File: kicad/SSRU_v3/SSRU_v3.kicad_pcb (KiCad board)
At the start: 2 copper layers, 100 x 100 mm, 115 parts, among them J1 AVR-ISP-6, J10 Conn_01x04, J11 Conn_01x02, J20 Conn_01x02, J21 Conn_01x02, J22 Conn_01x04, J23 Conn_01x02, J24 Conn_01x04, J25 Conn_01x02, J26 Conn_01x03, J27 Conn_01x03, J3 Conn_01x02, J30 Conn_01x02, J31 Conn_01x04, J32 Conn_01x04, J4 Conn_01x02, J5 Conn_01x02, SW1 SW_Push, U1 MCP2515-xSO, U10 TJA1051T, U11 Ai-Thinker-Ra-02, U12 TJA1051T, U13 CH340N, U2 ATmega328P-A, U3 TXS0102DCT, U4 LM2576S-5, U5 AMS1117-3.3, U6 LM324, U7 MCP2515-xSO, U8 74LVC1G17, U9 MT3608/SDB628, Y1 16MHz, Y3 16MHz, Y4 16MHz

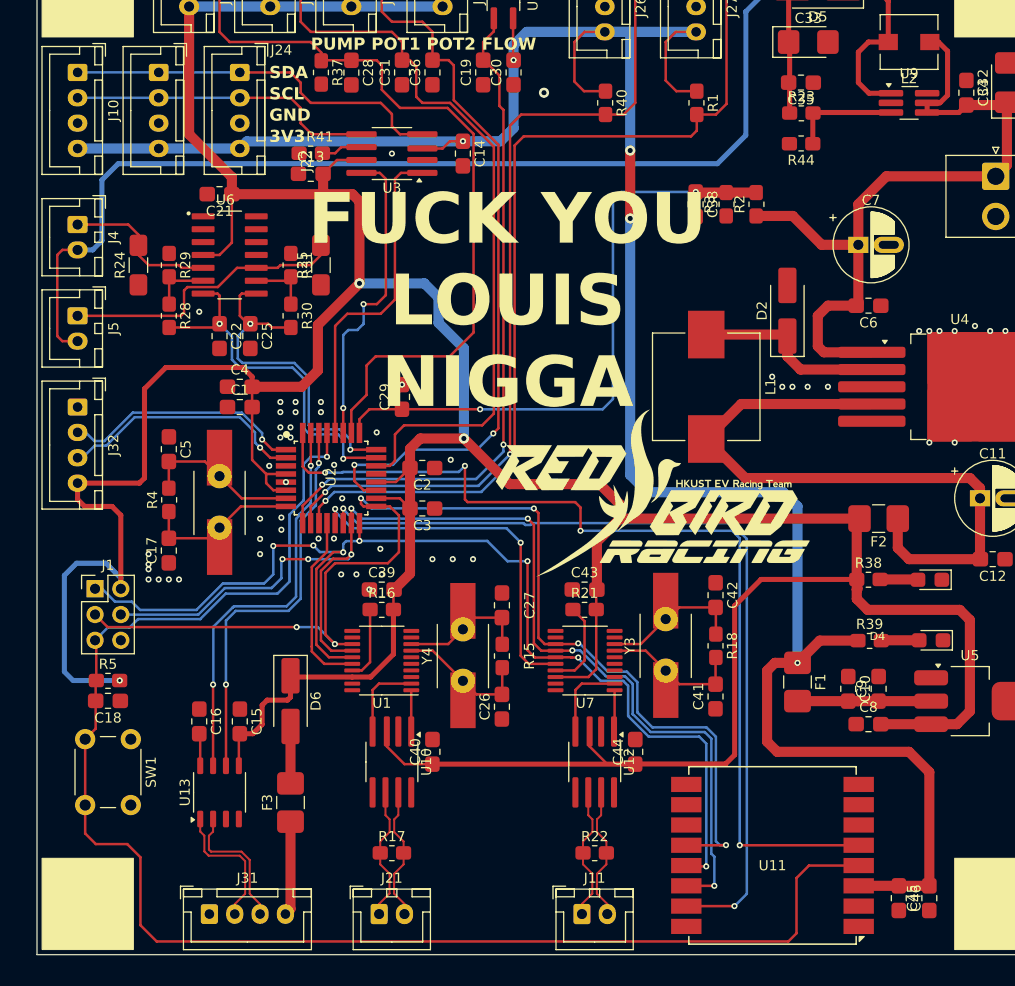
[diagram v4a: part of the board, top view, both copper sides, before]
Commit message: created TS schematics
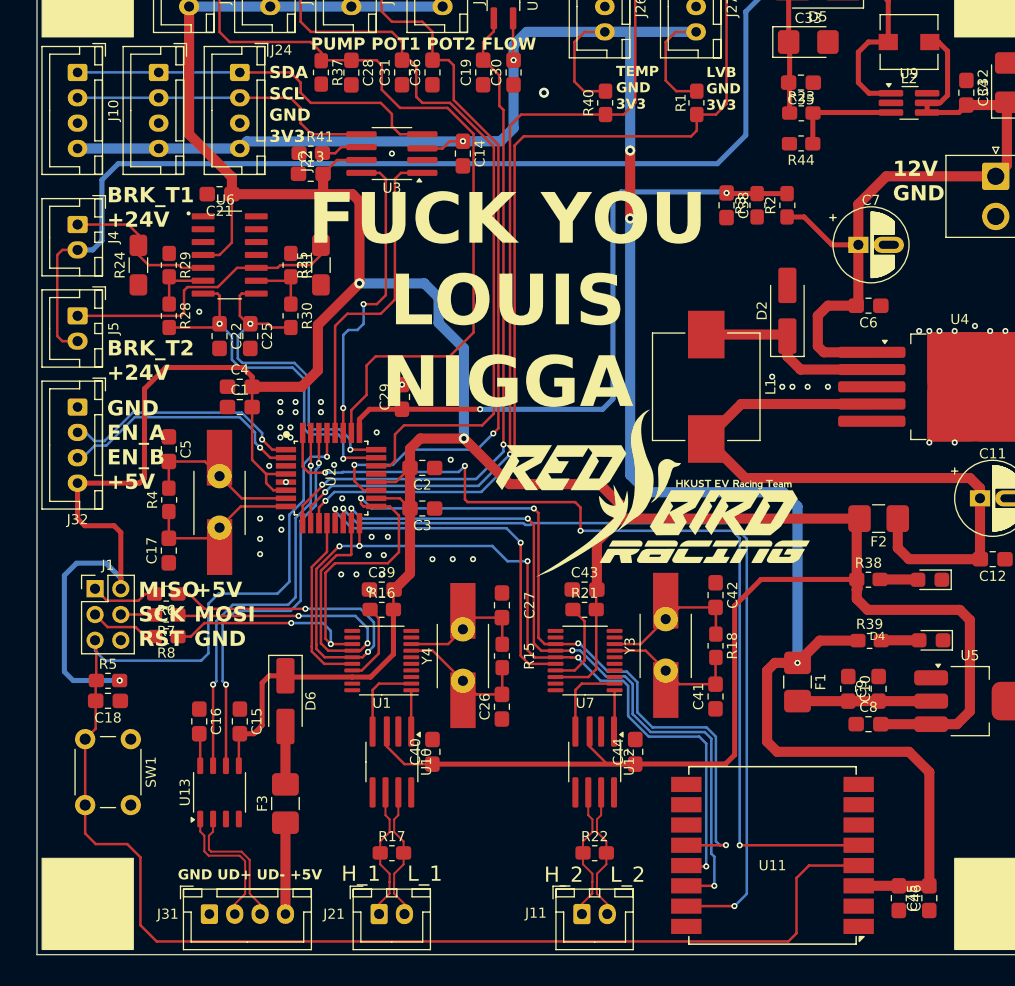
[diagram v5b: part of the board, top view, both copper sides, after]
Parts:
- added R6: 4.7k, RMC_Resistor:R_0805_2012Metric_Pad1.20x1.40mm_HandSolder_L, F.Cu at (112.7, 114.4)
- added R7: 4.7k, RMC_Resistor:R_0805_2012Metric_Pad1.20x1.40mm_HandSolder_L, F.Cu at (112.7, 116.5)
- added R8: 4.7k, RMC_Resistor:R_0805_2012Metric_Pad1.20x1.40mm_HandSolder_L, F.Cu at (112.7, 118.6)
- moved C38 3.05 mm to (168.0, 76.1)
- moved R2 3.05 mm to (174.0, 76.1)
- moved R3 3.05 mm to (171.0, 76.1)
- moved F3 0.51 mm to (124.5, 135.1)
- moved D6 0.50 mm to (124.5, 125.0)
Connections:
- J1 pad 1: MISO -> Net-(J1-MISO)
- J1 pad 3: SCK -> Net-(J1-SCK)
- J1 pad 4: MOSI -> Net-(J1-MOSI)
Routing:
- net SCK: track 119.6 -> 112.2 mm
- net Net-(J1-SCK): track 0.00 -> 6.77 mm
- net Net-(J1-MISO): track 0.00 -> 6.64 mm
- net RST: track 149.2 -> 154.3 mm
- net MISO: track 112.6 -> 107.9 mm
- net MOSI: track 115.8 -> 112.2 mm, vias 7 -> 6
- net Net-(J1-MOSI): track 0.00 -> 3.34 mm
- net +12V: track 74.6 -> 71.5 mm
- net LVB_S: track 61.3 -> 64.3 mm
- net Net-(U1-~{RESET}): track 7.29 -> 7.99 mm
- net GND: vias 68 -> 62
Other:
- board text added: "+5V MOSI GND"
- board text added: "12V GND"
- board text added: "BRK_T1 +24V"
- board text added: "BRK_T2 +24V"
- board text added: "GND EN_A EN_B +5V"
- board text added: "GND UD+ UD- +5V"
- board text added: "H_1 L_1"
- board text added: "H_2 L_2"
- board text added: "LVB GND 3V3"
- board text added: "MISO SCK RST"
- board text added: "TEMP GND 3V3"

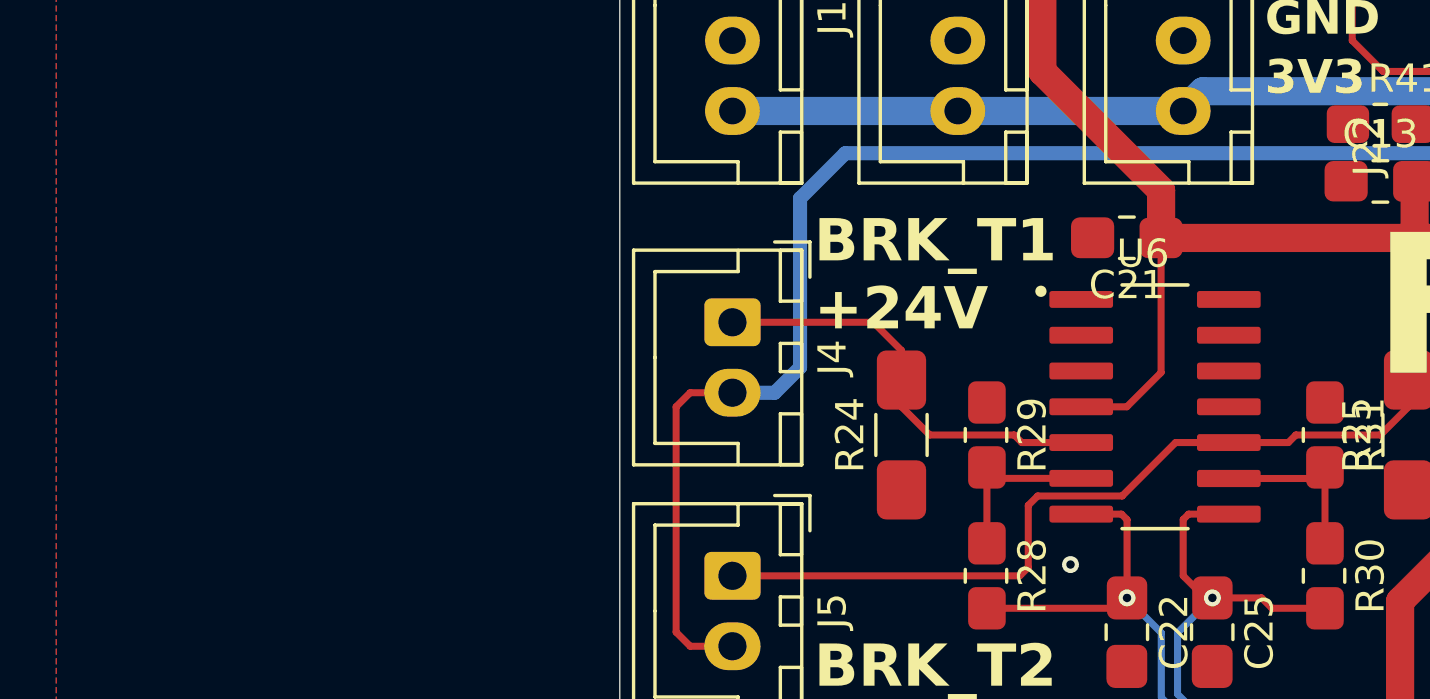
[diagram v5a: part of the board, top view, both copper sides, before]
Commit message: current to voltage
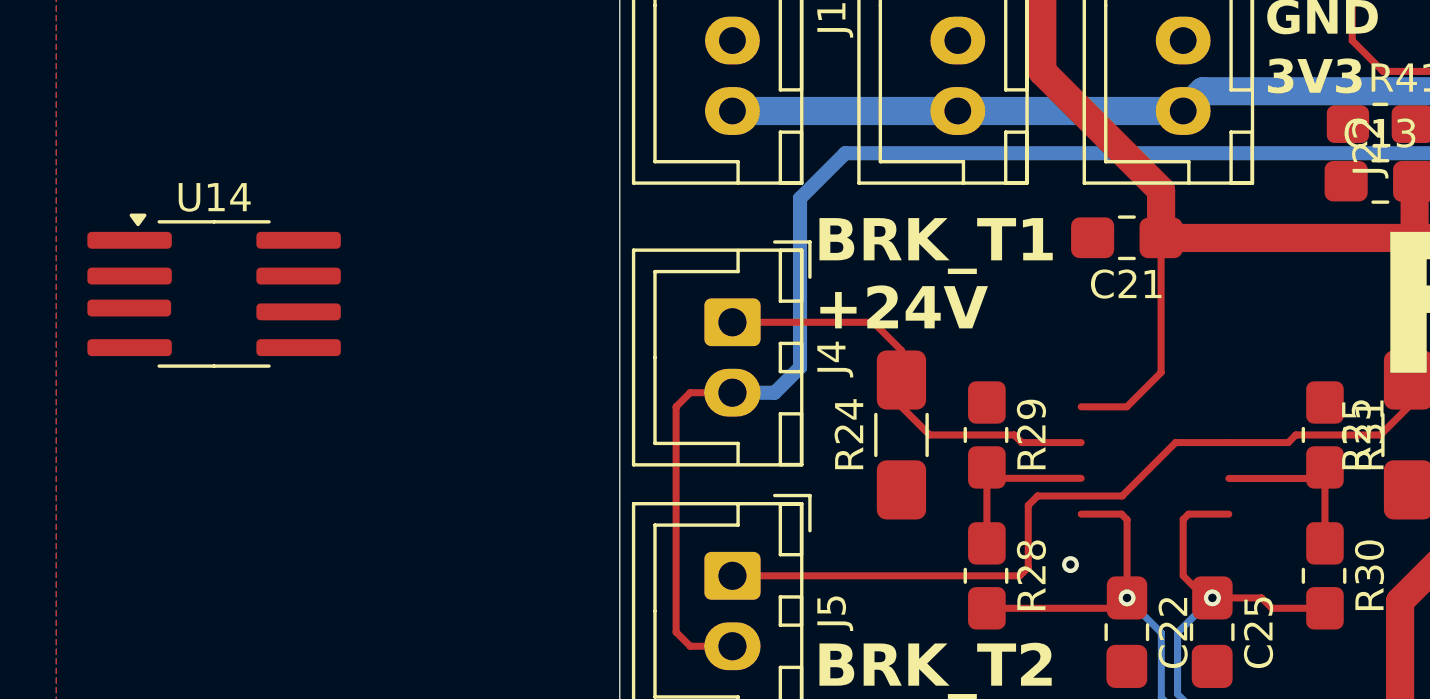
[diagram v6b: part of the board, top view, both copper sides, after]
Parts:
- removed U6: LM324, RMC_SO:SOIC127P600X175-14N
- added U14: LM2904, RMC_SO:SOIC-8_3.9x4.9mm_P1.27mm_RMC_Handsolder, F.Cu at (85.6, 77.0)

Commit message: SSRU V3
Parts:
- removed J10: Conn_01x04, Connector_JST:JST_XH_B4B-XH-A_1x04_P2.50mm_Vertical
- added G***: LOGO, LOGO, F.Cu at (147.0, 83.8)
- added G***: LOGO, LOGO, B.Cu at (150.0, 99.8)
- R28: value 5k -> 22k
- moved U14 33.5 mm to (119.0, 80.0), turned to 180 degrees
- moved C21 9.18 mm to (116.2, 84.0)
- moved J22 8.00 mm to (104.0, 63.0)
- moved J24 5.00 mm to (115.0, 63.0)
- moved G*** 4.24 mm to (157.0, 103.0)
- moved C41 0.93 mm to (166.0, 124.7)
- moved C42 0.93 mm to (166.0, 114.7)
- moved R18 0.93 mm to (166.0, 119.7)
- moved C26 0.85 mm to (145.9, 124.7)
- moved C27 0.85 mm to (145.9, 114.7)
- moved R15 0.85 mm to (145.9, 119.7)
- moved Y4 0.81 mm to (142.0, 122.2)
- moved R28 0.53 mm to (112.5, 87.0)
- moved R29 0.53 mm to (112.5, 82.0)
- moved R24 0.50 mm to (109.5, 82.0)
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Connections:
- R28 pad 1: Net-(U14A--) -> Net-(U14B--)
- R29 pad 2: Net-(U14A--) -> Net-(U14B--)
- R30 pad 1: Net-(U14B--) -> Net-(U14A--)
- R31 pad 2: Net-(U14B--) -> Net-(U14A--)
- U14 pad 1: BRAKE_TEMP_OUT1 -> BRAKE_TEMP_OUT2
- U14 pad 3: BRAKE_TEMP1 -> BRAKE_TEMP2
- U14 pad 5: BRAKE_TEMP2 -> BRAKE_TEMP1
- U14 pad 7: BRAKE_TEMP_OUT2 -> BRAKE_TEMP_OUT1
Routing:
- net Net-(U5-VO): track 14.2 -> 41.2 mm
- net BRAKE_TEMP_OUT1: track 36.0 -> 42.5 mm
- net SCL_3V3: track 30.4 -> 34.5 mm
- net BRAKE_TEMP_OUT2: track 33.9 -> 37.7 mm
- net Net-(U14B--): track 6.27 -> 8.81 mm
- net Net-(U14A--): track 6.20 -> 8.32 mm
- net BRAKE_TEMP2: track 28.7 -> 30.8 mm, vias 0 -> 1
- net +5V: track 432.3 -> 434.3 mm, vias 3 -> 6
- net SDA_3V3: track 37.8 -> 38.5 mm
- net Net-(U1-OSC2): track 13.4 -> 12.8 mm
- net GND: vias 62 -> 178
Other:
- board text added: "USSR v3"
- board text removed: "FUCK YOU LOUIS NIGGA"
